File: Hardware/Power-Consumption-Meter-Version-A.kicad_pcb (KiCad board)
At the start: 2 copper layers, 99.1 x 113 mm, 36 parts, among them J1 Jack_DC, J10 01x02, J11 01x02, J12 01x02, J13 01x02, J2 BAT_IN, J3 PWR_BTN, J4 USB_A, J5 Jack_DC, J6 Jack_DC, J7 USB_B_Mini, J8 USB_B_Micro, J9 01x04, SW1 SW_Slide, SW2 SW_Push, U1 Arduino_Nano_v3.x, U2 Display_5641BS, U3 INA219_Module

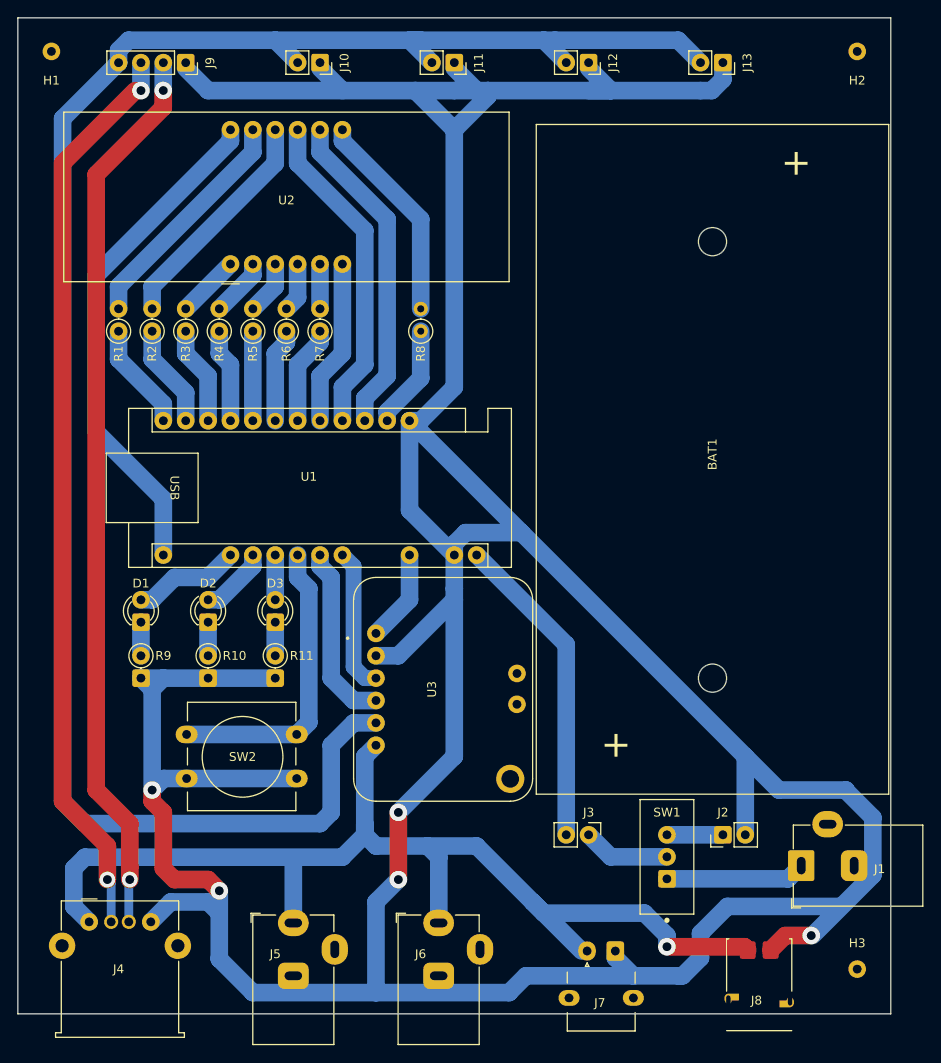
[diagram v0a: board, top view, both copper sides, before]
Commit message: Version B: adding case 3D model
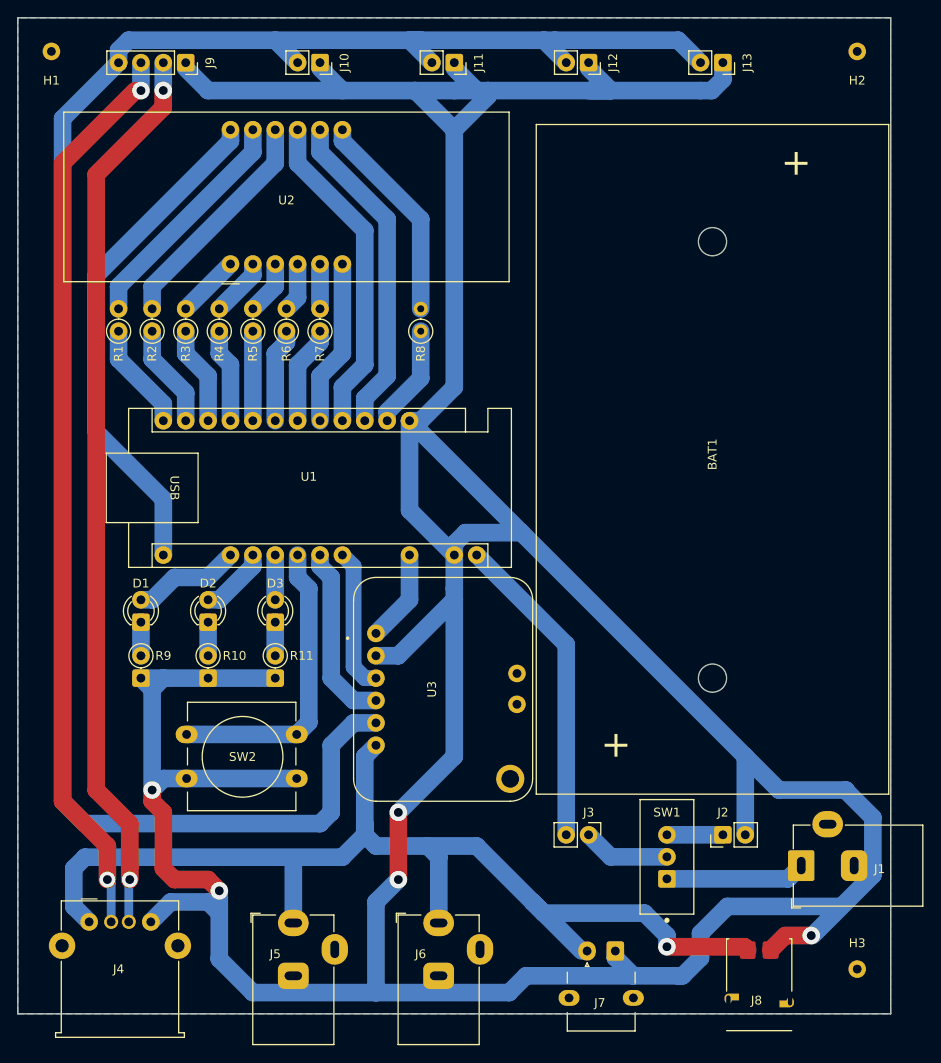
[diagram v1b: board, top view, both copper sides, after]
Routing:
- added copper zone on B.Cu, net GND
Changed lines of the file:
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@@
 		(net 41)
+	)
+	(zone
+		(net 7)
+		(net_name "GND")
+		(layer "B.Cu")
+		(name "GND")
+		(hatch edge 0.5)
+		(connect_pads yes
+			(clearance 1)
+		)
+		(min_thickness 0.25)
+		(filled_areas_thickness no)
+		(fill yes
+			(thermal_gap 0.5)
+			(thermal_bridge_width 0.5)
+		)
+		(polygon
+			(pts
+				(xy 96.52 33.02) (xy 96.52 146.05) (xy 195.58 146.05) (xy 195.58 33.02)
+			)
+		)
 	)
 	(embedded_fonts no)
